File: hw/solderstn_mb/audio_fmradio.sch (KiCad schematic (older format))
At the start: 41 parts, among them J2001 Conn_01x02, J2002 Conn_01x02, J2003 Conn_01x02, J2004 SJ-3571N, J2005 Conn_01x02, U2001 Si4735-D60-GU, U2002 TS4990IDT, U2003 TS4990IDT

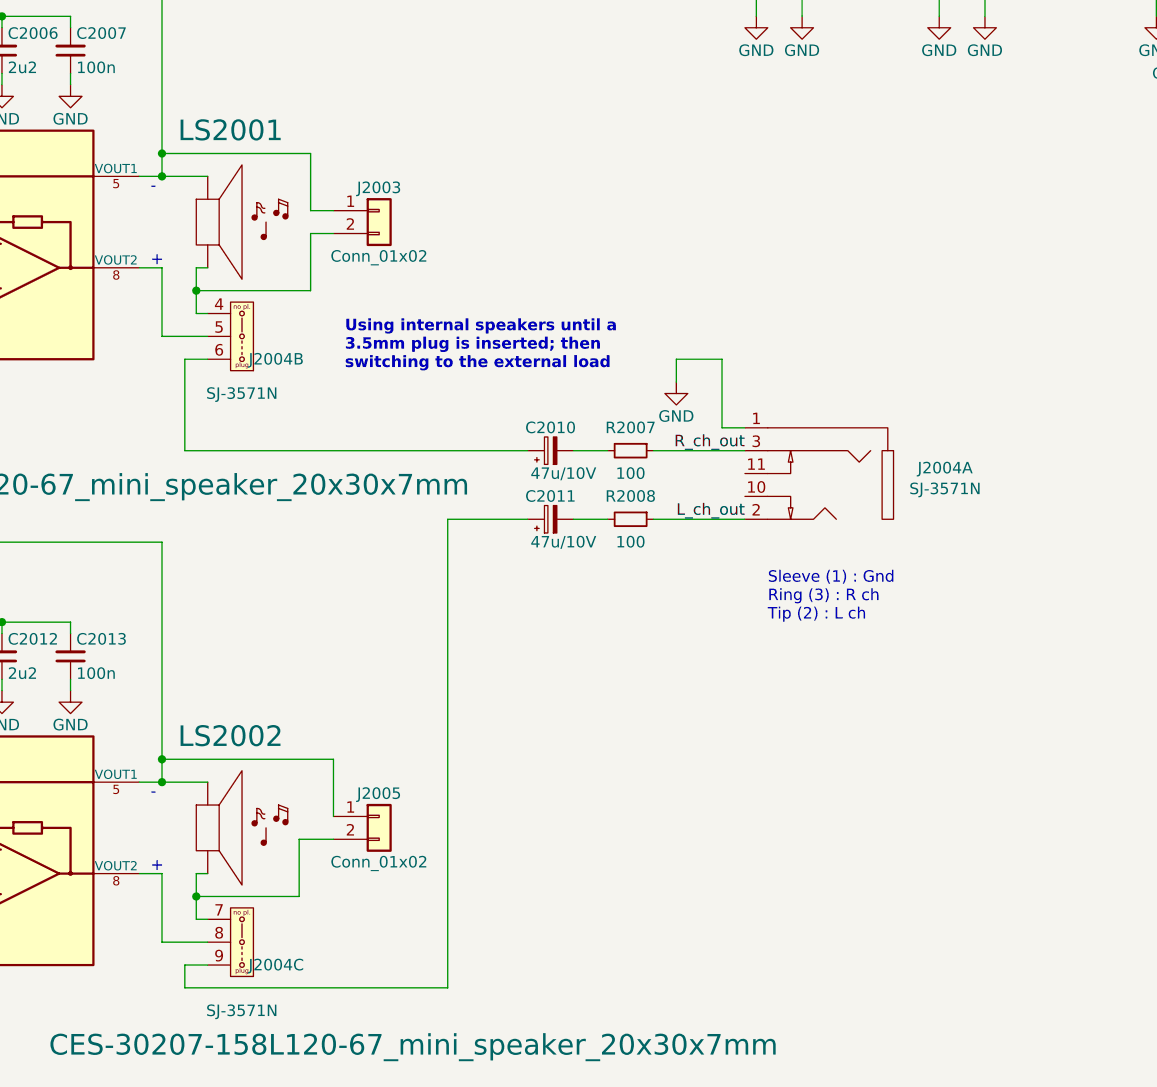
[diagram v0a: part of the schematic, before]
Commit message: * Remove separate REED_PULLUP_EN pin; instead bias the Reedswitches with the per-channel KTY bias (buffered Vref) * Add separate mini cut-out sub-PCB for 3.5 headphone connector at back-panel (must be angled vertical to fit in panel) * Some ESD and buffering on back panel
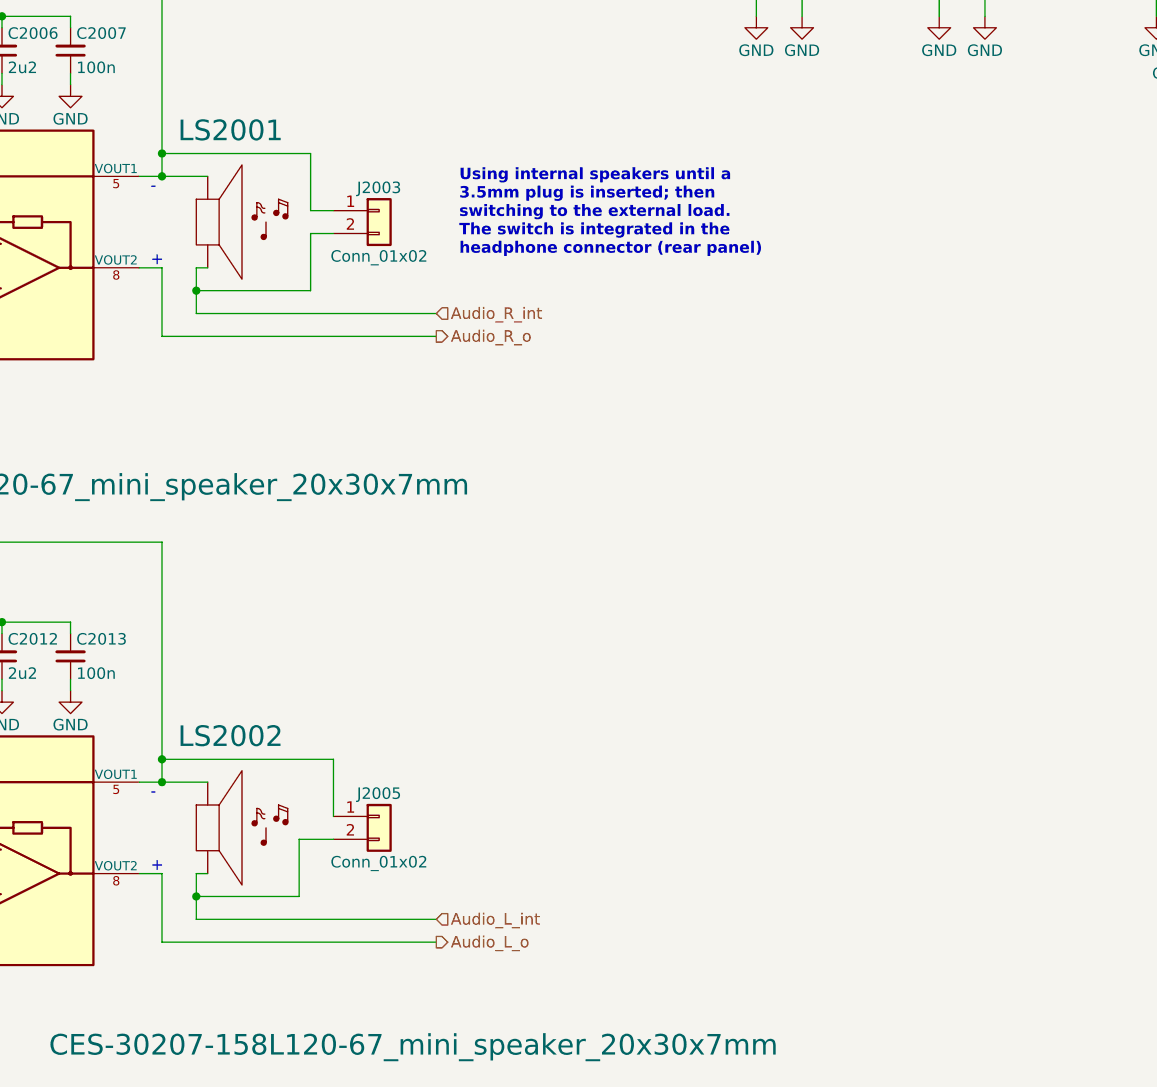
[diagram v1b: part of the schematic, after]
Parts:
- removed C2010, C2011: 47u/10V, symbol Device:CP_Small
- removed J2004: SJ-3571N, customlib_mj_fp:SJ-3571N, symbol customlib_mj:SJ-3571N
- removed R2007, R2008: 100, symbol Device:R_Small
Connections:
- net labels added: Audio_L_int, Audio_L_o, Audio_R_int, Audio_R_o
- net labels removed: L_ch_out, R_ch_out
- wire segments 161 -> 145
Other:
- note added: "Using internal speakers until a\n3.5mm plug is inserted; then\nswitching to the external load.\nThe switch is integrated in the\nheadphone connector (rear panel)"
- note removed: "Sleeve (1) : Gnd\nRing (3) : R ch\nTip (2) : L ch"
- note removed: "Using internal speakers until a\n3.5mm plug is inserted; then\nswitching to the external load"
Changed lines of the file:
@@
 $Descr A4 11693 8268
 encoding utf-8
-Sheet 20 21
+Sheet 21 22
 Title "Audio & FM-radio :)"
 Date "2020-08-12"
@@
 $EndComp
 $Comp
-L Device:R_Small R2007
-U 1 1 5F3C7C43
-P 5850 5000
-F 0 "R2007" V 5750 5000 50  0000 C CNN
-F 1 "100" V 5950 5000 50  0000 C CNN
-F 2 "" H 5850 5000 50  0001 C CNN
-F 3 "~" H 5850 5000 50  0001 C CNN
-	1    5850 5000
-	0    1    1    0
-$EndComp
-$Comp
 L Device:C_Small C2009
 U 1 1 5F3C8295
@@
 	1150 3700 1300 3700
 $Comp
-L Device:CP_Small C2010
-U 1 1 5F40B5B0
-P 5500 5000
-F 0 "C2010" V 5600 5000 50  0000 C CNN
-F 1 "47u/10V" V 5400 4800 50  0000 L CNN
-F 2 "" H 5500 5000 50  0001 C CNN
-F 3 "~" H 5500 5000 50  0001 C CNN
-	1    5500 5000
-	0    -1   -1   0
-$EndComp
-Wire Wire Line
-	5600 5000 5750 5000
-$Comp
 L customlib_mj:TS4990IDT U2003
 U 1 1 5F416928
@@
 $EndComp
 $Comp
-L Device:R_Small R2008
-U 1 1 5F41695A
-P 5850 5300
-F 0 "R2008" V 5750 5300 50  0000 C CNN
-F 1 "100" V 5950 5300 50  0000 C CNN
-F 2 "" H 5850 5300 50  0001 C CNN
-F 3 "~" H 5850 5300 50  0001 C CNN
-	1    5850 5300
-	0    1    1    0
-$EndComp
-$Comp
 L Device:C_Small C2015
 U 1 1 5F416964
@@
 	1150 6350 1300 6350
 $Comp
-L Device:CP_Small C2011
-U 1 1 5F4169C8
-P 5500 5300
-F 0 "C2011" V 5600 5300 50  0000 C CNN
-F 1 "47u/10V" V 5400 5100 50  0000 L CNN
-F 2 "" H 5500 5300 50  0001 C CNN
-F 3 "~" H 5500 5300 50  0001 C CNN
-	1    5500 5300
-	0    -1   -1   0
-$EndComp
-Wire Wire Line
-	5050 5300 5400 5300
-Wire Wire Line
-	5600 5300 5750 5300
-$Comp
 L Connector_Generic:Conn_01x02 J2002
 U 1 1 5F5B2BFC
@@
 Wire Wire Line
 	8900 2550 8800 2550
-$Comp
-L customlib_mj:SJ-3571N J2004
-U 1 1 5F5CEE99
-P 6650 5150
-F 0 "J2004" H 6074 5224 50  0000 C CNN
-F 1 "SJ-3571N" H 6074 5133 50  0000 C CNN
-F 2 "customlib_mj_fp:SJ-3571N" H 6650 5150 50  0001 C CNN
-F 3 "https://www.cuidevices.com/product/interconnect/connectors/audio-connectors/jacks/sj-357xn-series/sj-3571n" H 6650 5150 50  0001 C CNN
-	1    6650 5150
-	-1   0    0    -1
-$EndComp
-$Comp
-L customlib_mj:SJ-3571N J2004
-U 2 1 5F5D23CA
-P 4150 4500
-F 0 "J2004" H 4000 4400 50  0000 C CNN
-F 1 "SJ-3571N" H 4150 4250 50  0000 C CNN
-F 2 "customlib_mj_fp:SJ-3571N" H 4150 4500 50  0001 C CNN
-F 3 "https://www.cuidevices.com/product/interconnect/connectors/audio-connectors/jacks/sj-357xn-series/sj-3571n" H 4150 4500 50  0001 C CNN
-	2    4150 4500
-	-1   0    0    -1
-$EndComp
-$Comp
-L customlib_mj:SJ-3571N J2004
-U 3 1 5F5D3D4C
-P 4150 7150
-F 0 "J2004" H 4000 7050 50  0000 C CNN
-F 1 "SJ-3571N" H 4150 6850 50  0000 C CNN
-F 2 "customlib_mj_fp:SJ-3571N" H 4150 7150 50  0001 C CNN
-F 3 "https://www.cuidevices.com/product/interconnect/connectors/audio-connectors/jacks/sj-357xn-series/sj-3571n" H 4150 7150 50  0001 C CNN
-	3    4150 7150
-	-1   0    0    -1
-$EndComp
 Wire Wire Line
 	3700 4200 3800 4200
@@
 	3800 4200 3800 4500
 Wire Wire Line
-	3800 4500 4000 4500
+	3800 4500 5000 4500
 Wire Wire Line
 	3700 6850 3800 6850
@@
 	3800 6850 3800 7150
 Wire Wire Line
-	3800 7150 4000 7150
-Wire Wire Line
-	4000 7250 3900 7250
-Wire Wire Line
-	3900 7250 3900 7350
-Wire Wire Line
-	3900 7350 5050 7350
-Wire Wire Line
-	5050 7350 5050 5300
-Wire Wire Line
-	4000 4600 3900 4600
-Wire Wire Line
-	3900 5000 5400 5000
+	3800 7150 5000 7150
 Wire Wire Line
 	4000 6850 3950 6850
@@
 	3950 6850 3950 6950
 Wire Wire Line
-	3950 7050 4000 7050
+	3950 7050 5000 7050
 Wire Wire Line
 	4000 4200 3950 4200
@@
 	3950 4200 3950 4300
 Wire Wire Line
-	3950 4400 4000 4400
-Wire Wire Line
-	3900 4600 3900 5000
-Wire Wire Line
-	5950 5300 6350 5300
-Wire Wire Line
-	5950 5000 6350 5000
-Text Notes 6450 5750 0    50   ~ 0
-Sleeve (1) : Gnd\nRing (3) : R ch\nTip (2) : L ch
-$Comp
-L power:GND #PWR02020
-U 1 1 5F689124
-P 6050 4700
-F 0 "#PWR02020" H 6050 4450 50  0001 C CNN
-F 1 "GND" H 6050 4550 50  0000 C CNN
-F 2 "" H 6050 4700 50  0001 C CNN
-F 3 "" H 6050 4700 50  0001 C CNN
-	1    6050 4700
-	1    0    0    -1
-$EndComp
-Wire Wire Line
-	6350 4900 6250 4900
-Wire Wire Line
-	6250 4900 6250 4600
-Wire Wire Line
-	6250 4600 6050 4600
-Wire Wire Line
-	6050 4600 6050 4700
+	3950 4400 5000 4400
 Text Notes 1000 6000 0    50   ~ 10
 Left channel
 Text Notes 1000 3500 0    50   ~ 10
 Right channel
-Text Label 6350 5300 2    50   ~ 0
-L_ch_out
-Text Label 6350 5000 2    50   ~ 0
-R_ch_out
 $Comp
 L Connector_Generic:Conn_01x02 J2003
@@
 Wire Wire Line
 	3400 6050 3400 6000
-Text Notes 4600 4650 0    50   ~ 10
-Using internal speakers until a\n3.5mm plug is inserted; then\nswitching to the external load
+Text Notes 5100 4150 0    50   ~ 10
+Using internal speakers until a\n3.5mm plug is inserted; then\nswitching to the external load.\nThe switch is integrated in the\nheadphone connector (rear panel)
+Text HLabel 5000 4500 2    50   Output ~ 0
+Audio_R_o
+Text HLabel 5000 7150 2    50   Output ~ 0
+Audio_L_o
+Text HLabel 5000 4400 2    50   Input ~ 0
+Audio_R_int
+Text HLabel 5000 7050 2    50   Input ~ 0
+Audio_L_int
 $EndSCHEMATC

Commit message: * Added Molex connectors (PwrLED-conn, DC-in, FM-ant.) * Renamed Si4735 doc dir
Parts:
- added JP?: dogbone_2, symbol customlib_mj:dogbone_2
- J2002: value Conn_01x02 -> Molex_PicoBlade-53398-0271; footprint (none) -> Connector_Molex:Molex_PicoBlade_53398-0271_1x02-1MP_P1.25mm_Vertical
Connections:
- wire segments 145 -> 147
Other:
- note added: "(OTS cable assm: e.g. 151340203)"
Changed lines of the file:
@@
 Text Notes 10350 2650 0    50   ~ 10
 To ferrite loop stick,\napprx 180-450µH
-Text Notes 8650 2950 0    50   ~ 10
+Text Notes 8700 3000 0    50   ~ 10
 To e.g. 1/4 FM wire-\nor screw telescope\n(whip) antenna
 $Comp
@@
 U 1 1 5F5B2BFC
 P 9100 2450
-F 0 "J2002" H 9200 2450 50  0000 L CNN
-F 1 "Conn_01x02" H 9410 2351 50  0000 C CNN
-F 2 "" H 9100 2450 50  0001 C CNN
-F 3 "~" H 9100 2450 50  0001 C CNN
+F 0 "J2002" H 9100 2250 50  0000 C CNN
+F 1 "Molex_PicoBlade-53398-0271" H 9100 2550 50  0000 C CNN
+F 2 "Connector_Molex:Molex_PicoBlade_53398-0271_1x02-1MP_P1.25mm_Vertical" H 9100 2450 50  0001 C CNN
+F 3 "https://www.molex.com/molex/products/part-detail/pcb_headers/0533980271" H 9100 2450 50  0001 C CNN
 	1    9100 2450
 	1    0    0    -1
@@
 L power:GND #PWR02008
 U 1 1 5F5B3589
-P 8800 2550
-F 0 "#PWR02008" H 8800 2300 50  0001 C CNN
-F 1 "GND" H 8800 2400 50  0000 C CNN
-F 2 "" H 8800 2550 50  0001 C CNN
-F 3 "" H 8800 2550 50  0001 C CNN
-	1    8800 2550
-	1    0    0    -1
-$EndComp
-Wire Wire Line
-	8900 2550 8800 2550
+P 8550 2600
+F 0 "#PWR02008" H 8550 2350 50  0001 C CNN
+F 1 "GND" H 8550 2450 50  0000 C CNN
+F 2 "" H 8550 2600 50  0001 C CNN
+F 3 "" H 8550 2600 50  0001 C CNN
+	1    8550 2600
+	1    0    0    -1
+$EndComp
 Wire Wire Line
 	3700 4200 3800 4200
@@
 Wire Wire Line
 	3800 3700 3800 3800
-$Comp
-L customlib_mj:CES-30207-158L120-67_mini_speaker_20x30x7mm LS2001
-U 1 1 5F6F74E3
-P 4000 4000
-F 0 "LS2001" H 4100 4400 90  0000 C CNN
-F 1 "CES-30207-158L120-67_mini_speaker_20x30x7mm" H 3550 2850 90  0000 C CNN
-F 2 "Connector_Molex:Molex_PicoBlade_53398-0271_1x02-1MP_P1.25mm_Vertical" H 4000 4000 90  0001 C CNN
-F 3 "https://www.cuidevices.com/product/audio/speakers/miniature-(10-mm~40-mm)/ces-30207-158l120-67" H 4000 4000 90  0001 C CNN
-	1    4000 4000
-	1    0    0    -1
-$EndComp
 $Comp
 L customlib_mj:CES-30207-158L120-67_mini_speaker_20x30x7mm LS2002
@@
 Text HLabel 5000 7050 2    50   Input ~ 0
 Audio_L_int
+$Comp
+L customlib_mj:CES-30207-158L120-67_mini_speaker_20x30x7mm LS2001
+U 1 1 5F6F74E3
+P 4000 4000
+F 0 "LS2001" H 4100 4400 90  0000 C CNN
+F 1 "CES-30207-158L120-67_mini_speaker_20x30x7mm" H 3550 2850 90  0000 C CNN
+F 2 "Connector_Molex:Molex_PicoBlade_53398-0271_1x02-1MP_P1.25mm_Vertical" H 4000 4000 90  0001 C CNN
+F 3 "https://www.cuidevices.com/product/audio/speakers/miniature-(10-mm~40-mm)/ces-30207-158l120-67" H 4000 4000 90  0001 C CNN
+	1    4000 4000
+	1    0    0    -1
+$EndComp
+Text Notes 8450 2300 0    50   ~ 0
+(OTS cable assm: e.g. 151340203)
+$Comp
+L customlib_mj:dogbone_2 JP?
+U 1 1 5FB8DE1A
+P 8750 2550
+F 0 "JP?" H 8650 2475 50  0000 L CNN
+F 1 "dogbone_2" H 8750 2650 50  0001 C CNN
+F 2 "" H 8750 2550 50  0001 C CNN
+F 3 "" H 8750 2550 50  0001 C CNN
+	1    8750 2550
+	1    0    0    -1
+$EndComp
+Wire Wire Line
+	8550 2600 8550 2550
+Wire Wire Line
+	8550 2550 8650 2550
+Wire Wire Line
+	8850 2550 8900 2550
 $EndSCHEMATC

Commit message: Updated display-board sch & PCB with optional left-hand rotary encoder instead of pwrbtn. Printed MB schematic updates PDF for 20-08-21
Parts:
- gave numbers to parts that had none: 1
- renumbered C2001 to C2101, C2002 to C2102, C2003 to C2103, C2004 to C2104, C2005 to C2105, C2006 to C2106, C2007 to C2107, C2008 to C2108, C2009 to C2109, C2012 to C2110, C2013 to C2111, C2014 to C2112, C2015 to C2113, D2001 to D2101, D2002 to D2102, J2001 to J2101, J2002 to J2102, J2003 to J2103, J2005 to J2104, JP2001 to JP2101, JP2002 to JP2102, L2001 to L2101, LS2001 to LS2101, LS2002 to LS2102, R2001 to R2101, R2002 to R2102, R2003 to R2103, R2004 to R2104, R2005 to R2105, R2006 to R2106, R2009 to R2107, R2010 to R2108, R2011 to R2109, U2001 to U2101, U2002 to U2102, U2003 to U2103

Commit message: Corrected several ERC issues. Re-annotated & assigned all footprints except 32k xtal (will prob. replace with RTC module anyway)
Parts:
- removed JP2101: dogbone_3, symbol customlib_mj:dogbone_3
- removed JP2102, JP2103: dogbone_2, symbol customlib_mj:dogbone_2
- added JP2101: dogbone_3_ud, customlib_mj_fp:db3_ud_0402, symbol customlib_mj:dogbone_3_ud
- added JP2102, JP2103: dogbone_2_ud, customlib_mj_fp:db2_ud_0402, symbol customlib_mj:dogbone_2_ud
- C2101, C2102, C2103, C2104, C2105, C2106, C2107, C2108, C2109, C2110, C2111, C2112, C2113: footprint (none) -> Capacitor_SMD:C_0603_1608Metric
- J2101, J2103, J2104: footprint (none) -> Connector_PinHeader_2.54mm:PinHeader_1x02_P2.54mm_Vertical
- R2101, R2102, R2103, R2104, R2105, R2106, R2107, R2108, R2109: footprint (none) -> Resistor_SMD:R_0603_1608Metric
- U2102, U2103: footprint (none) -> Package_SO:SO-8_3.9x4.9mm_P1.27mm
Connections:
- wire segments 147 -> 159
- no-connect marks 1 -> 3

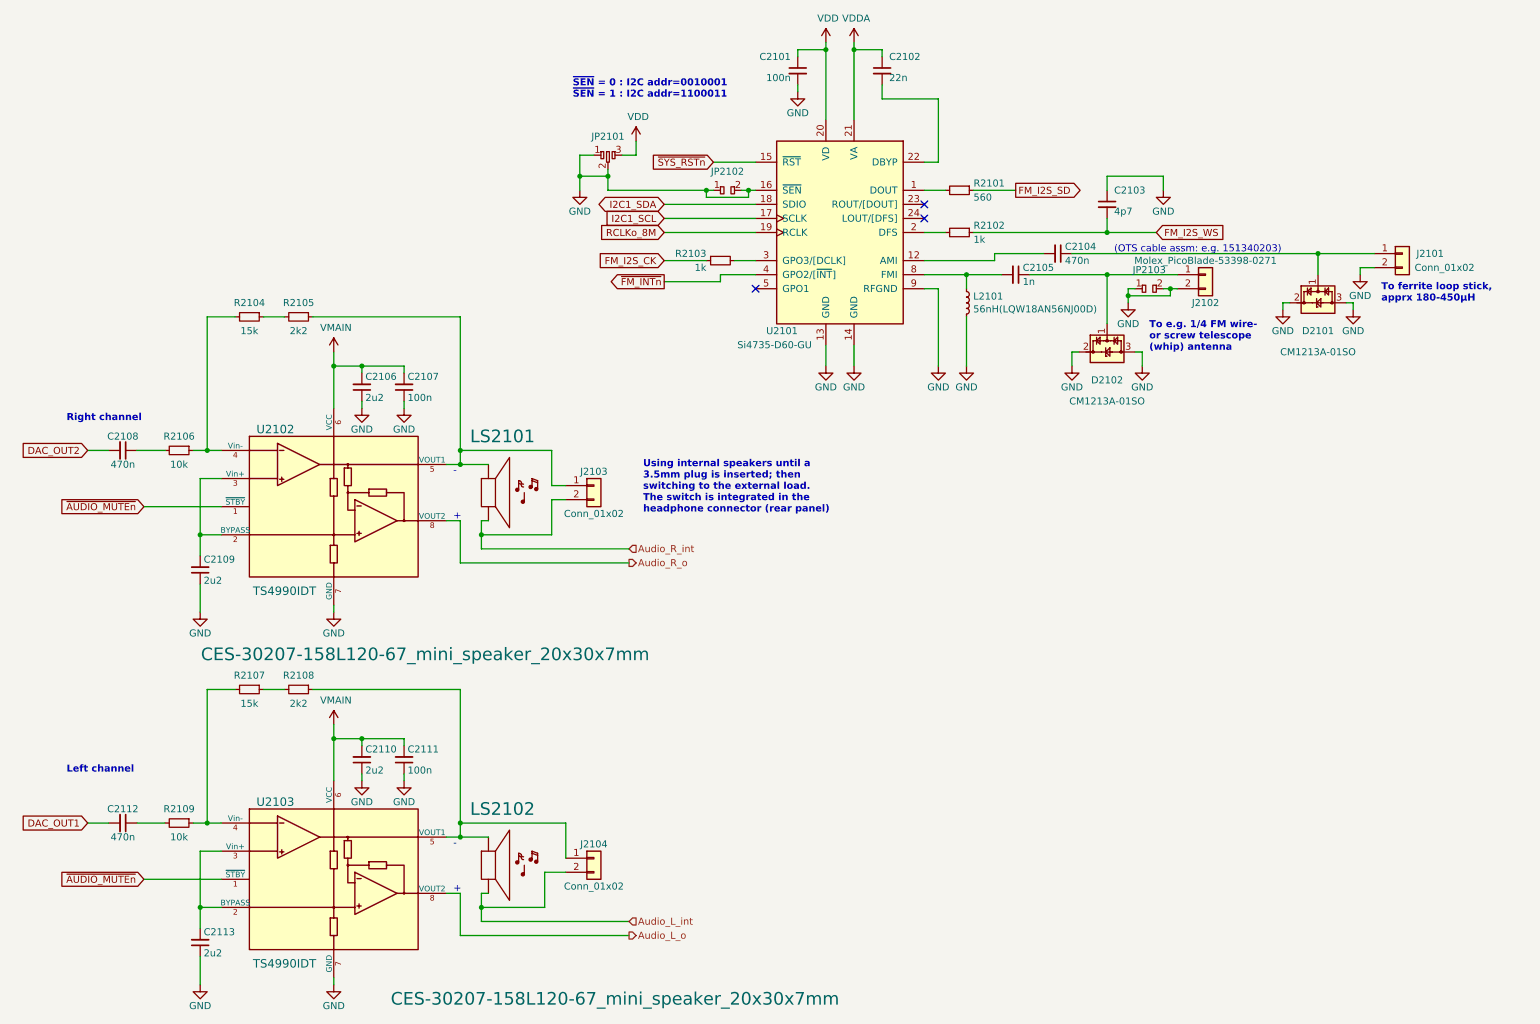
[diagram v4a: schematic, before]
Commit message: *) Cut-out in MB for Schaffner FN283 AC-jack; re-generated MB 3d, import into assembly-testing *) Re-gen & Imported Kicad Backpanel into asm-testing. *) docs for new CUI internal speakers
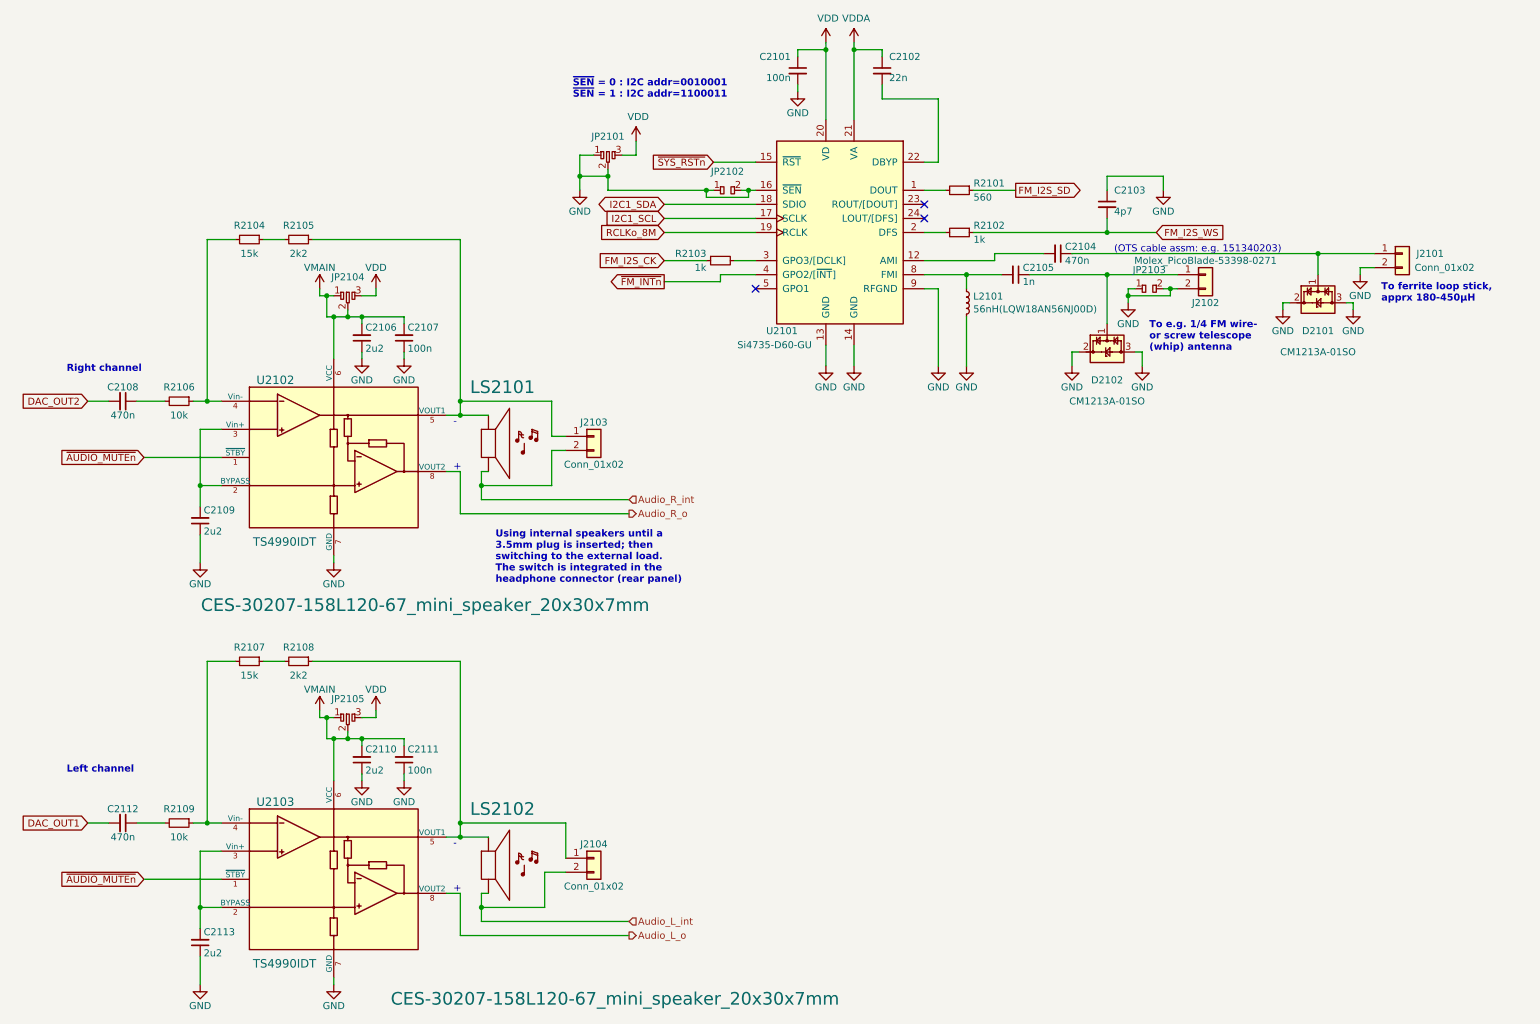
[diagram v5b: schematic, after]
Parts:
- added JP2104, JP2105: dogbone_3_ud, customlib_mj_fp:db3_ud_0402, symbol customlib_mj:dogbone_3_ud
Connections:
- net VDD: now also JP2104.3, JP2105.3
- net VMAIN: now also JP2104.1, JP2104.2, JP2105.1, JP2105.2
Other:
- moved on the sheet: C2106, C2107, C2108, C2109, J2103, LS2101, R2104, R2105, R2106, R2107, R2108, U2102
